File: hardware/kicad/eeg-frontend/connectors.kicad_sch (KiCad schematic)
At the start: 4 parts, among them J1 EEG Connector, J2 Conn_02x06_Top_Bottom, J3 Conn_01x08, J4 Conn_01x02

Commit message: Assign footprints to schematic components
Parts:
- J1: footprint (none) -> Connector_PinHeader_2.54mm:PinHeader_2x13_P2.54mm_Horizontal
- J2: footprint (none) -> myLibrary:PinHeader_2x06_P2.54mm_Horizontal_pmod
- J3: footprint (none) -> Connector_PinSocket_2.54mm:PinSocket_1x08_P2.54mm_Vertical
- J4: footprint (none) -> Connector_PinSocket_2.54mm:PinSocket_1x02_P2.54mm_Vertical
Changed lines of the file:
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@@
 			)
 		)
-		(property "Footprint" ""
+		(property "Footprint" "Connector_PinSocket_2.54mm:PinSocket_1x02_P2.54mm_Vertical"
 			(at 66.04 157.48 0)
 			(hide yes)
@@
 			)
 		)
-		(property "Footprint" ""
+		(property "Footprint" "Connector_PinSocket_2.54mm:PinSocket_1x08_P2.54mm_Vertical"
 			(at 66.04 140.97 0)
 			(hide yes)
@@
 			)
 		)
-		(property "Footprint" ""
+		(property "Footprint" "Connector_PinHeader_2.54mm:PinHeader_2x13_P2.54mm_Horizontal"
 			(at 55.88 95.25 0)
 			(hide yes)
@@
 			)
 		)
-		(property "Footprint" ""
+		(property "Footprint" "myLibrary:PinHeader_2x06_P2.54mm_Horizontal_pmod"
 			(at 55.88 41.91 0)
 			(hide yes)

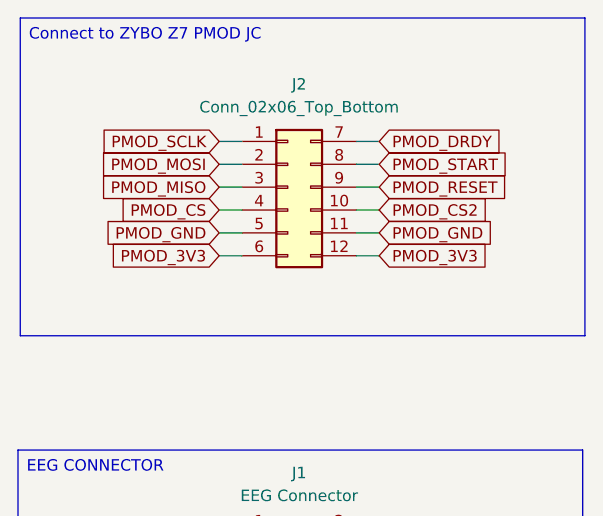
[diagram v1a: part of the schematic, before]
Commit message: 一旦できたと思ったPCB。 しかしPMODのコネクタの位置が左右で逆で、このまま刺すとGNDの一に通常のデータ信号的なのが来てしまう。
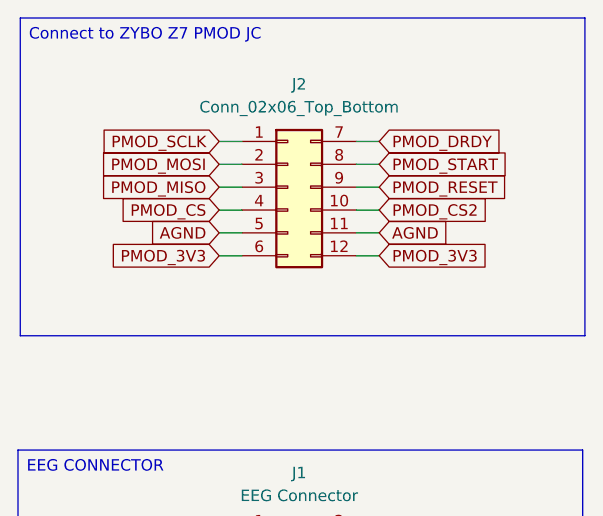
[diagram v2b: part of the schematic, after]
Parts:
- J1: footprint Connector_PinHeader_2.54mm:PinHeader_2x13_P2.54mm_Horizontal -> myLibrary:PinHeader_2x13_P2.54mm_Horizontal_mirror
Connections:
- net PMOD_GND is gone; now on net AGND: J2.11 (Pin_11), J2.5 (Pin_5)
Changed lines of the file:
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@@
 		)
 	)
-	(global_label "PMOD_GND"
+	(global_label "AGND"
 		(shape input)
 		(at 66.04 46.99 0)
@@
 		)
 		(property "Intersheetrefs" "${INTERSHEET_REFS}"
-			(at 79.1852 46.99 0)
+			(at 73.9843 46.99 0)
 			(hide yes)
 			(show_name no)
@@
 		)
 	)
-	(global_label "PMOD_GND"
+	(global_label "AGND"
 		(shape input)
 		(at 48.26 46.99 180)
@@
 		)
 		(property "Intersheetrefs" "${INTERSHEET_REFS}"
-			(at 35.1148 46.99 0)
+			(at 40.3157 46.99 0)
 			(hide yes)
 			(show_name no)
@@
 			)
 		)
-		(property "Footprint" "Connector_PinHeader_2.54mm:PinHeader_2x13_P2.54mm_Horizontal"
+		(property "Footprint" "myLibrary:PinHeader_2x13_P2.54mm_Horizontal_mirror"
 			(at 55.88 95.25 0)
 			(hide yes)
